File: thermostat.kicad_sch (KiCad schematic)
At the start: 103 parts, among them U17 AD5680, U18 AD7172-2, U19 AD7172-4BCPZ, U20 RS8552, U21 MAX1968xUI

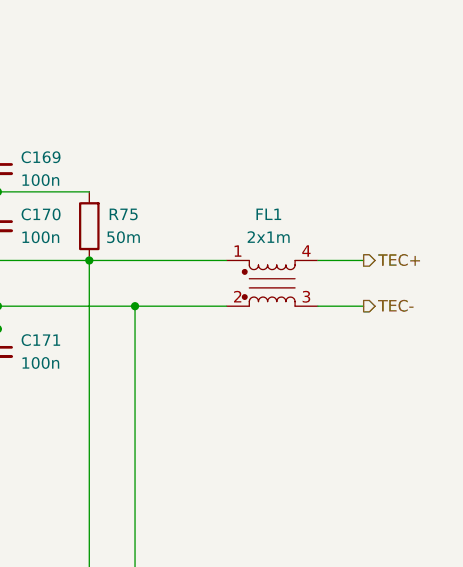
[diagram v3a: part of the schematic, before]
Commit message: sch: Fix incorrect TEC polarity in thermostat - Fix Issue #27
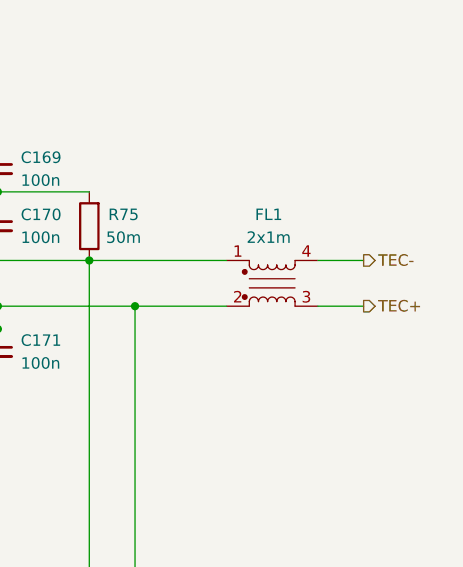
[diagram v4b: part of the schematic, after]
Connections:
- net TEC+: now also FL1.3; no longer FL1.4
- net TEC-: now also FL1.4; no longer FL1.3
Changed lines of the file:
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@@
+    (stroke (width 0) (type default))
+  )
+  (wire (pts (xy 176.53 96.52) (xy 181.61 96.52))
+    (stroke (width 0) (type default))
+  )
+  (wire (pts (xy 271.78 149.86) (xy 267.97 149.86))
+    (stroke (width 0) (type default))
+  )
+  (wire (pts (xy 182.88 188.595) (xy 190.5 188.595))
+    (stroke (width 0) (type default))
+  )
+  (wire (pts (xy 262.89 137.16) (xy 262.89 139.7))
+    (stroke (width 0) (type default))
+  )
+  (wire (pts (xy 345.44 101.6) (xy 345.44 144.78))
+    (stroke (width 0) (type default))
+  )
+  (wire (pts (xy 326.39 144.78) (xy 328.93 144.78))
+    (stroke (width 0) (type default))
+  )
+  (wire (pts (xy 283.21 144.78) (xy 267.97 144.78))
+    (stroke (width 0) (type default))
+  )
+  (wire (pts (xy 247.65 193.675) (xy 247.65 188.595))
+    (stroke (width 0) (type default))
+  )
+  (wire (pts (xy 184.15 71.12) (xy 196.85 71.12))
+    (stroke (width 0) (type default))
+  )
+  (wire (pts (xy 311.15 101.6) (xy 345.44 101.6))
+    (stroke (width 0) (type default))
+  )
+  (wire (pts (xy 234.95 149.86) (xy 234.95 147.32))
+    (stroke (width 0) (type default))
+  )
+  (wire (pts (xy 96.52 124.46) (xy 107.95 124.46))
+    (stroke (width 0) (type default))
+  )
+  (wire (pts (xy 240.03 208.915) (xy 252.73 208.915))
+    (stroke (width 0) (type default))
+  )
+  (wire (pts (xy 234.315 276.225) (xy 234.315 277.495))
+    (stroke (width 0) (type default))
+  )
+  (wire (pts (xy 267.97 232.41) (xy 267.97 238.125))
+    (stroke (width 0) (type default))
+  )
+  (wire (pts (xy 335.28 106.68) (xy 350.52 106.68))
+    (stroke (width 0) (type default))
+  )
+  (wire (pts (xy 182.88 193.675) (xy 190.5 193.675))
+    (stroke (width 0) (type default))
+  )
+  (wire (pts (xy 325.12 95.25) (xy 325.12 93.98))
+    (stroke (width 0) (type default))
+  )
+  (wire (pts (xy 154.305 264.795) (xy 184.15 264.795))
+    (stroke (width 0) (type default))
+  )
+  (wire (pts (xy 348.615 196.215) (xy 356.235 196.215))
+    (stroke (width 0) (type default))
+  )
+  (wire (pts (xy 120.65 268.605) (xy 120.65 245.745))
+    (stroke (width 0) (type default))
+  )
+  (wire (pts (xy 199.39 88.9) (xy 201.93 88.9))
+    (stroke (width 0) (type default))
+  )
+  (wire (pts (xy 335.28 100.33) (xy 335.28 106.68))
+    (stroke (width 0) (type default))
+  )
+  (wire (pts (xy 224.79 277.495) (xy 234.315 277.495))
+    (stroke (width 0) (type default))
+  )
+  (wire (pts (xy 93.98 93.98) (xy 96.52 93.98))
+    (stroke (width 0) (type default))
+  )
+  (wire (pts (xy 264.16 130.81) (xy 262.89 130.81))
+    (stroke (width 0) (type default))
+  )
+  (wire (pts (xy 325.12 88.9) (xy 326.39 88.9))
+    (stroke (width 0) (type default))
+  )
+  (wire (pts (xy 250.19 162.56) (xy 271.78 162.56))
+    (stroke (width 0) (type default))
+  )
+  (wire (pts (xy 322.58 132.08) (xy 328.93 132.08))
+    (stroke (width 0) (type default))
+  )
+  (wire (pts (xy 273.685 232.41) (xy 273.685 240.665))
+    (stroke (width 0) (type default))
+  )
+  (wire (pts (xy 83.82 62.23) (xy 83.82 64.77))
+    (stroke (width 0) (type default))
+  )
+  (wire (pts (xy 161.29 222.885) (xy 161.29 224.155))
+    (stroke (width 0) (type default))
+  )
+  (wire (pts (xy 80.01 217.805) (xy 92.71 217.805))
+    (stroke (width 0) (type default))
+  )
+  (wire (pts (xy 307.975 196.215) (xy 332.105 196.215))
+    (stroke (width 0) (type default))
+  )
+  (wire (pts (xy 264.16 111.76) (xy 290.83 111.76))
+    (stroke (width 0) (type default))
+  )
+  (wire (pts (xy 247.015 262.255) (xy 259.715 262.255))
+    (stroke (width 0) (type default))
+  )
+  (wire (pts (xy 167.64 88.9) (xy 181.61 88.9))
+    (stroke (width 0) (type default))
+  )
+  (wire (pts (xy 246.38 147.32) (xy 250.19 147.32))
+    (stroke (width 0) (type default))
+  )
+  (wire (pts (xy 247.015 276.225) (xy 247.015 277.495))
+    (stroke (width 0) (type default))
+  )
+  (wire (pts (xy 267.97 188.595) (xy 267.97 224.79))
+    (stroke (width 0) (type default))
+  )
+  (wire (pts (xy 53.34 187.325) (xy 63.5 187.325))
+    (stroke (width 0) (type default))
+  )
+  (wire (pts (xy 240.03 222.885) (xy 240.03 224.155))
+    (stroke (width 0) (type default))
+  )
+  (wire (pts (xy 110.49 268.605) (xy 120.65 268.605))
+    (stroke (width 0) (type default))
+  )
+  (wire (pts (xy 177.165 240.665) (xy 184.15 240.665))
     (stroke (width 0) (type default))
   )
@@
     (stroke (width 0) (type default))
   )
-  (wire (pts (xy 176.53 96.52) (xy 181.61 96.52))
-    (stroke (width 0) (type default))
-  )
-  (wire (pts (xy 271.78 149.86) (xy 267.97 149.86))
-    (stroke (width 0) (type default))
-  )
-  (wire (pts (xy 182.88 188.595) (xy 190.5 188.595))
-    (stroke (width 0) (type default))
-  )
-  (wire (pts (xy 262.89 137.16) (xy 262.89 139.7))
-    (stroke (width 0) (type default))
-  )
-  (wire (pts (xy 345.44 101.6) (xy 345.44 144.78))
-    (stroke (width 0) (type default))
-  )
-  (wire (pts (xy 326.39 144.78) (xy 328.93 144.78))
-    (stroke (width 0) (type default))
-  )
-  (wire (pts (xy 283.21 144.78) (xy 267.97 144.78))
-    (stroke (width 0) (type default))
-  )
-  (wire (pts (xy 247.65 193.675) (xy 247.65 188.595))
-    (stroke (width 0) (type default))
-  )
-  (wire (pts (xy 184.15 71.12) (xy 196.85 71.12))
-    (stroke (width 0) (type default))
-  )
-  (wire (pts (xy 311.15 101.6) (xy 345.44 101.6))
-    (stroke (width 0) (type default))
-  )
-  (wire (pts (xy 234.95 149.86) (xy 234.95 147.32))
-    (stroke (width 0) (type default))
-  )
-  (wire (pts (xy 96.52 124.46) (xy 107.95 124.46))
-    (stroke (width 0) (type default))
-  )
-  (wire (pts (xy 240.03 208.915) (xy 252.73 208.915))
-    (stroke (width 0) (type default))
-  )
-  (wire (pts (xy 234.315 276.225) (xy 234.315 277.495))
-    (stroke (width 0) (type default))
-  )
-  (wire (pts (xy 267.97 232.41) (xy 267.97 238.125))
-    (stroke (width 0) (type default))
-  )
-  (wire (pts (xy 335.28 106.68) (xy 350.52 106.68))
-    (stroke (width 0) (type default))
-  )
-  (wire (pts (xy 182.88 193.675) (xy 190.5 193.675))
-    (stroke (width 0) (type default))
-  )
-  (wire (pts (xy 325.12 95.25) (xy 325.12 93.98))
-    (stroke (width 0) (type default))
-  )
-  (wire (pts (xy 154.305 264.795) (xy 184.15 264.795))
-    (stroke (width 0) (type default))
-  )
-  (wire (pts (xy 348.615 196.215) (xy 356.235 196.215))
-    (stroke (width 0) (type default))
-  )
-  (wire (pts (xy 120.65 268.605) (xy 120.65 245.745))
-    (stroke (width 0) (type default))
-  )
-  (wire (pts (xy 199.39 88.9) (xy 201.93 88.9))
-    (stroke (width 0) (type default))
-  )
-  (wire (pts (xy 335.28 100.33) (xy 335.28 106.68))
-    (stroke (width 0) (type default))
-  )
-  (wire (pts (xy 224.79 277.495) (xy 234.315 277.495))
-    (stroke (width 0) (type default))
-  )
-  (wire (pts (xy 93.98 93.98) (xy 96.52 93.98))
-    (stroke (width 0) (type default))
-  )
-  (wire (pts (xy 264.16 130.81) (xy 262.89 130.81))
-    (stroke (width 0) (type default))
-  )
-  (wire (pts (xy 325.12 88.9) (xy 326.39 88.9))
-    (stroke (width 0) (type default))
-  )
-  (wire (pts (xy 250.19 162.56) (xy 271.78 162.56))
-    (stroke (width 0) (type default))
-  )
-  (wire (pts (xy 322.58 132.08) (xy 328.93 132.08))
-    (stroke (width 0) (type default))
-  )
-  (wire (pts (xy 273.685 232.41) (xy 273.685 240.665))
-    (stroke (width 0) (type default))
-  )
-  (wire (pts (xy 83.82 62.23) (xy 83.82 64.77))
-    (stroke (width 0) (type default))
-  )
-  (wire (pts (xy 161.29 222.885) (xy 161.29 224.155))
-    (stroke (width 0) (type default))
-  )
-  (wire (pts (xy 80.01 217.805) (xy 92.71 217.805))
-    (stroke (width 0) (type default))
-  )
-  (wire (pts (xy 307.975 196.215) (xy 332.105 196.215))
-    (stroke (width 0) (type default))
-  )
-  (wire (pts (xy 264.16 111.76) (xy 290.83 111.76))
-    (stroke (width 0) (type default))
-  )
-  (wire (pts (xy 247.015 262.255) (xy 259.715 262.255))
-    (stroke (width 0) (type default))
-  )
-  (wire (pts (xy 167.64 88.9) (xy 181.61 88.9))
-    (stroke (width 0) (type default))
-  )
-  (wire (pts (xy 246.38 147.32) (xy 250.19 147.32))
-    (stroke (width 0) (type default))
-  )
-  (wire (pts (xy 247.015 276.225) (xy 247.015 277.495))
-    (stroke (width 0) (type default))
-  )
-  (wire (pts (xy 267.97 188.595) (xy 267.97 224.79))
-    (stroke (width 0) (type default))
-  )
-  (wire (pts (xy 53.34 187.325) (xy 63.5 187.325))
-    (stroke (width 0) (type default))
-  )
-  (wire (pts (xy 240.03 222.885) (xy 240.03 224.155))
-    (stroke (width 0) (type default))
-  )
-  (wire (pts (xy 110.49 268.605) (xy 120.65 268.605))
-    (stroke (width 0) (type default))
-  )
-  (wire (pts (xy 177.165 240.665) (xy 184.15 240.665))
-    (stroke (width 0) (type default))
-  )
   (wire (pts (xy 201.93 88.9) (xy 201.93 86.36))
     (stroke (width 0) (type default))
@@
     (stroke (width 0) (type default))
   )
+  (wire (pts (xy 370.84 106.68) (xy 375.92 106.68))
+    (stroke (width 0) (type default))
+  )
   (wire (pts (xy 252.73 99.06) (xy 290.83 99.06))
     (stroke (width 0) (type default))
   )
-  (wire (pts (xy 370.84 106.68) (xy 375.92 106.68))
-    (stroke (width 0) (type default))
-  )
   (wire (pts (xy 328.93 157.48) (xy 328.93 149.86))
     (stroke (width 0) (type default))
@@
     (effects (font (size 1.27 1.27)) (justify right))
   )
-  (hierarchical_label "TEC+" (shape output) (at 375.92 101.6 0) (fields_autoplaced)
+  (hierarchical_label "TEC+" (shape output) (at 375.92 106.68 0) (fields_autoplaced)
     (effects (font (size 1.27 1.27)) (justify left))
   )
@@
     (effects (font (size 1.27 1.27)) (justify left))
   )
-  (hierarchical_label "TEC-" (shape output) (at 375.92 106.68 0) (fields_autoplaced)
+  (hierarchical_label "TEC-" (shape output) (at 375.92 101.6 0) (fields_autoplaced)
     (effects (font (size 1.27 1.27)) (justify left))
   )

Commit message: sch: Update Title Block Info - rev0.3 -> rev0_3 - Correct the title of each schematics - Update the modified time
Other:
- company: M-Labs -> M-Labs Limited
- title: Kirdy -> thermostat
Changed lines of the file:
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@@
   (paper "A3")
   (title_block
-    (title "Kirdy")
-    (date "2022-07-03")
-    (rev "r0.3")
-    (company "M-Labs")
+    (title "thermostat")
+    (date "2023-11-09")
+    (rev "r0_3")
+    (company "M-Labs Limited")
     (comment 1 "Linus Woo Chun Kit")
   )

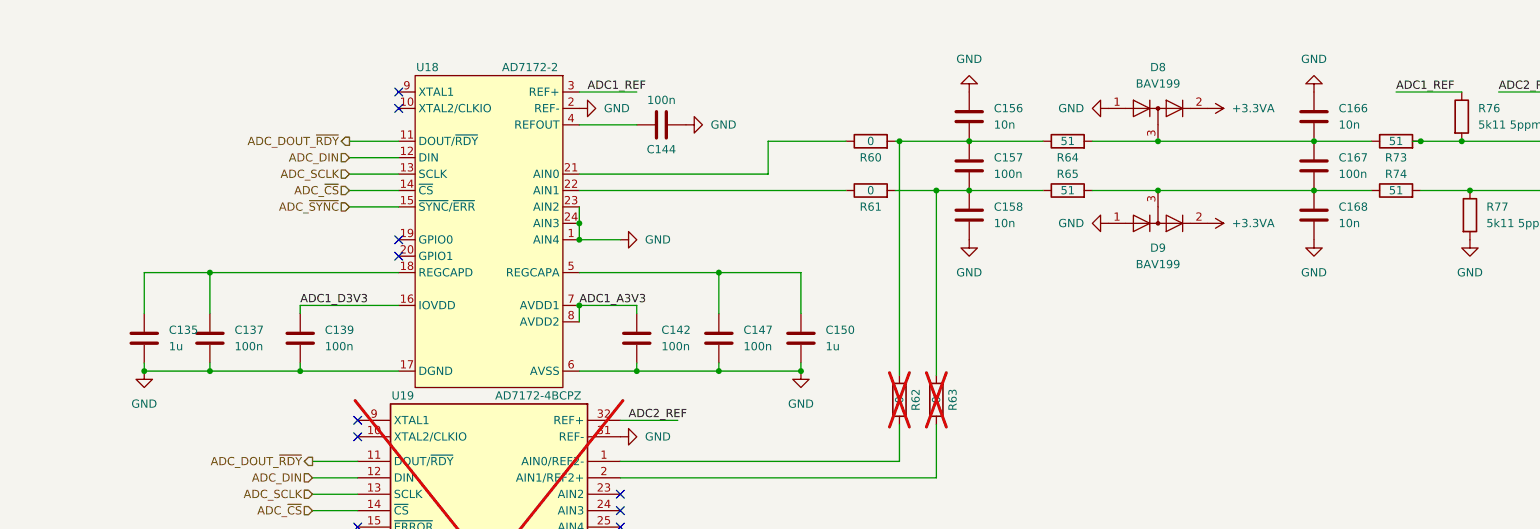
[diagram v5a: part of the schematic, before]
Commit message: sch, pcb: Correct MFR/PN and optimize BOM
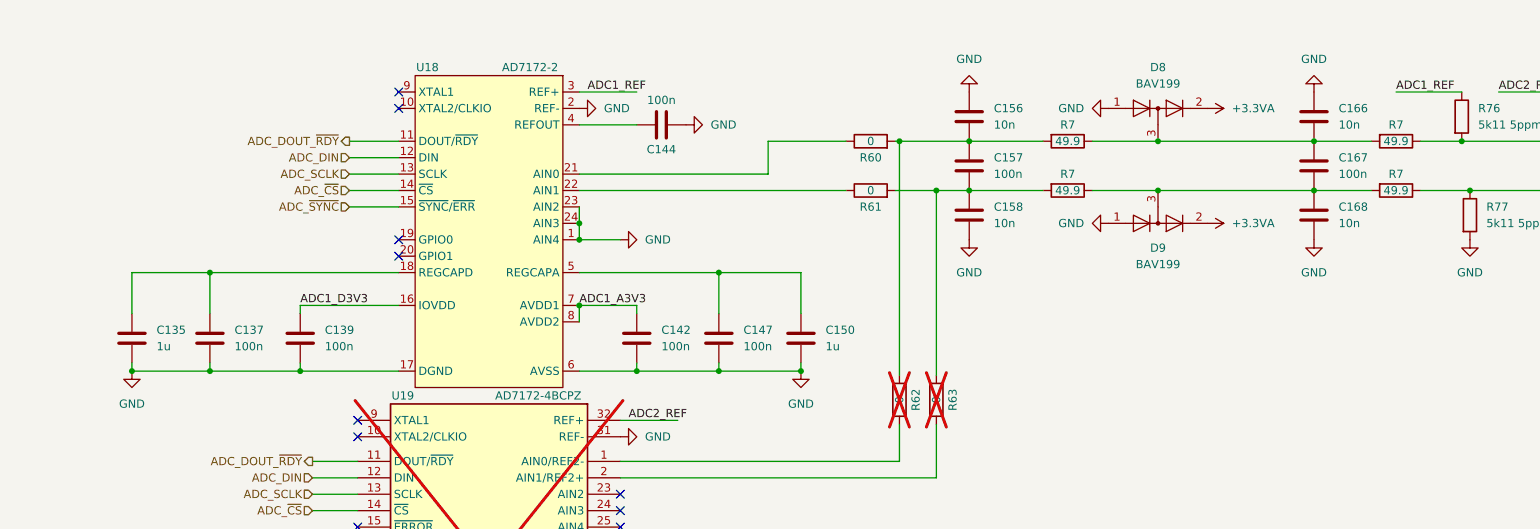
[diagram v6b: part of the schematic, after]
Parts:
- removed R64, R65, R73, R74: 51, Resistor_SMD:R_0603_1608Metric, symbol Device:R
- added R7 (x4): 49.9, Resistor_SMD:R_0603_1608Metric, symbol Device:R
- D8, D9: MFR_PN_ALT BAV199E6327HTSA1 -> BAV199LT1G
- R75: MFR_PN_ALT WSLT2010R5000FEA18 -> WSL2010R0500FEA18
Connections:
- net NTC+: now also R7.1
- net NTC-: now also R7.1
- net at C157.2, C158.1, R61.2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: now also R7.2
- net at C156.2, C157.1, R60.2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: now also R7.2
- net at C166.2, C167.1, D8.3 (K): now also R7.1, R7.2
- net at C167.2, C168.1, D9.3 (K): now also R7.1, R7.2
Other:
- moved on the sheet: C135

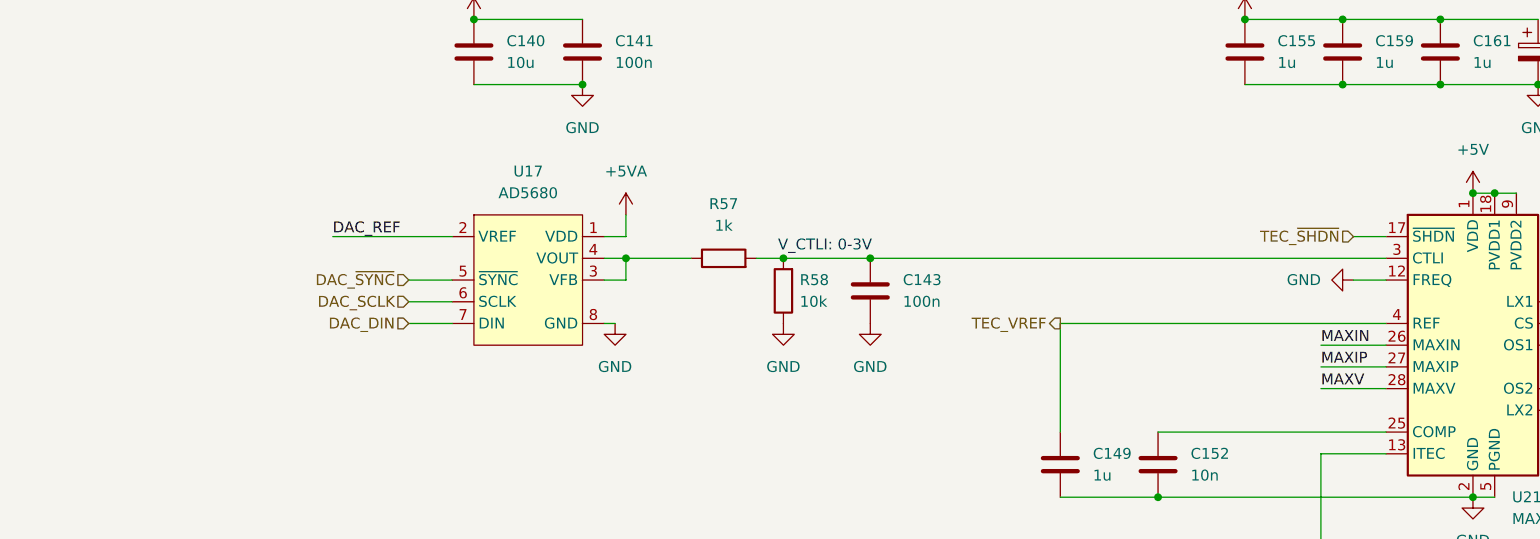
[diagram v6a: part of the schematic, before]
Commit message: sch, pcb: add 0R for TEC Vref Ouput - For debugging if needed
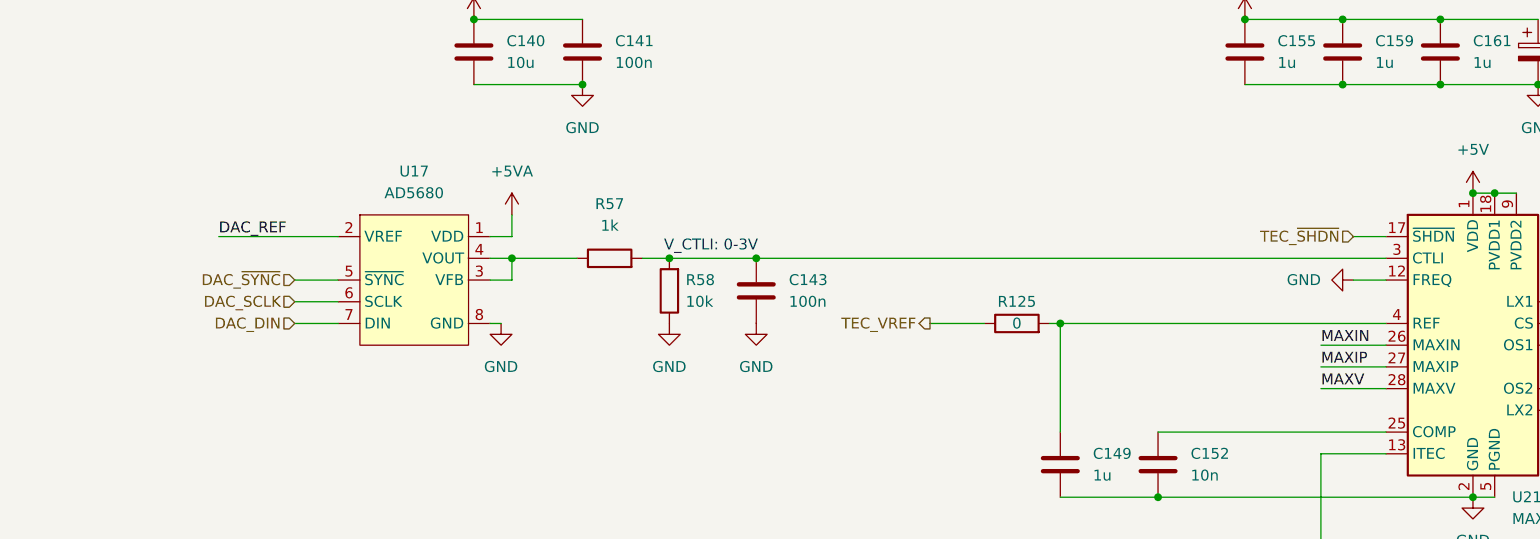
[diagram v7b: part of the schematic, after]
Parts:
- added R125: 0, Resistor_SMD:R_0603_1608Metric, symbol Device:R
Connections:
- net TEC_VREF: now also R125.1; no longer C149.1, U21.4 (REF)
- new net: C149.1, R125.2, U21.4 (REF)
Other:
- moved on the sheet: C143, R57, R58, U17

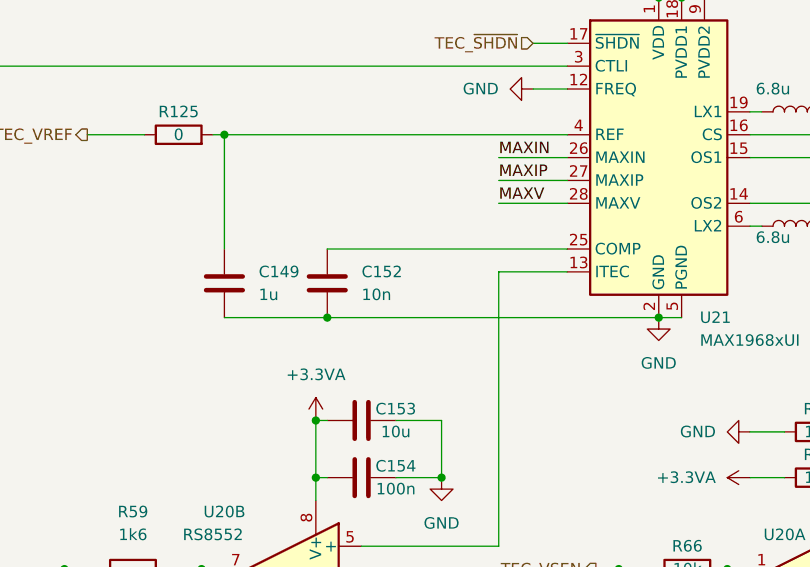
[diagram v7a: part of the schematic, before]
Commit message: sch, pcb: Remove X7R, X5R at input LT304x - Reduce the number of Tantalum Capacitor Used - Replace some non critical ones with Electrolytic Caps
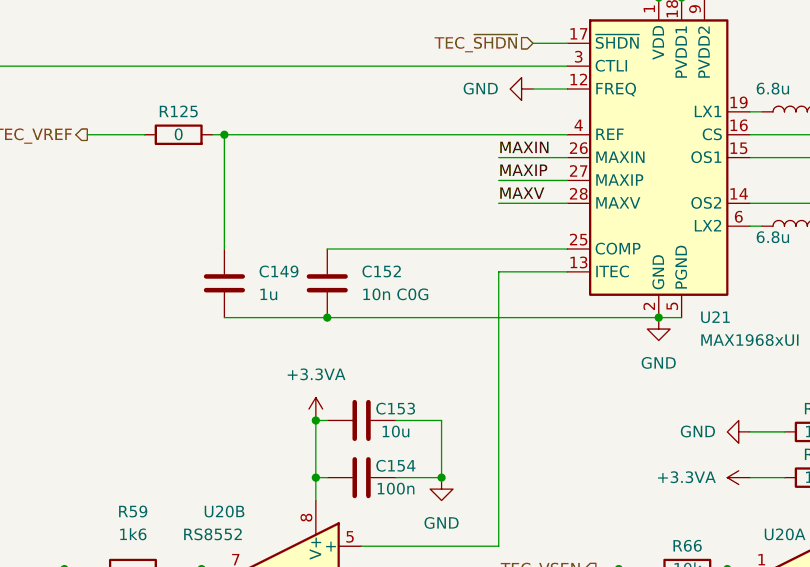
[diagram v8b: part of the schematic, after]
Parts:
- C152: value 10n -> 10n C0G; MFR_PN 0603B103K500CT -> GRM1885C1H103JA01J; MFR_PN_ALT CL10B103KB8NNNC -> (none)
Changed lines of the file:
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@@
   (symbol (lib_id "Device:C") (at 264.16 115.57 0) (unit 1)
     (in_bom yes) (on_board yes) (dnp no) (fields_autoplaced)
-    (property "Reference" "C152" (at 267.97 114.2999 0)
+    (property "Reference" "C152" (at 267.97 114.3 0)
       (effects (font (size 1.27 1.27)) (justify left))
     )
-    (property "Value" "10n" (at 267.97 116.8399 0)
+    (property "Value" "10n C0G" (at 267.97 116.84 0)
       (effects (font (size 1.27 1.27)) (justify left))
     )
@@
       (effects (font (size 1.27 1.27)) hide)
     )
-    (property "MFR_PN" "0603B103K500CT" (at 264.16 115.57 0)
+    (property "MFR_PN" "GRM1885C1H103JA01J" (at 264.16 115.57 0)
       (effects (font (size 1.27 1.27)) hide)
     )
-    (property "MFR_PN_ALT" "CL10B103KB8NNNC" (at 264.16 115.57 0)
+    (property "MFR_PN_ALT" "" (at 264.16 115.57 0)
       (effects (font (size 1.27 1.27)) hide)
     )
